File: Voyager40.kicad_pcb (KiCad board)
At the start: 2 copper layers, 244.5 x 76.2 mm, 192 parts, among them Q1 2N7002, SW1 5.2x5.2mm, U1 ATmega32U2-AU, U2 PRTR5V0U2X, Y1 16Mhz

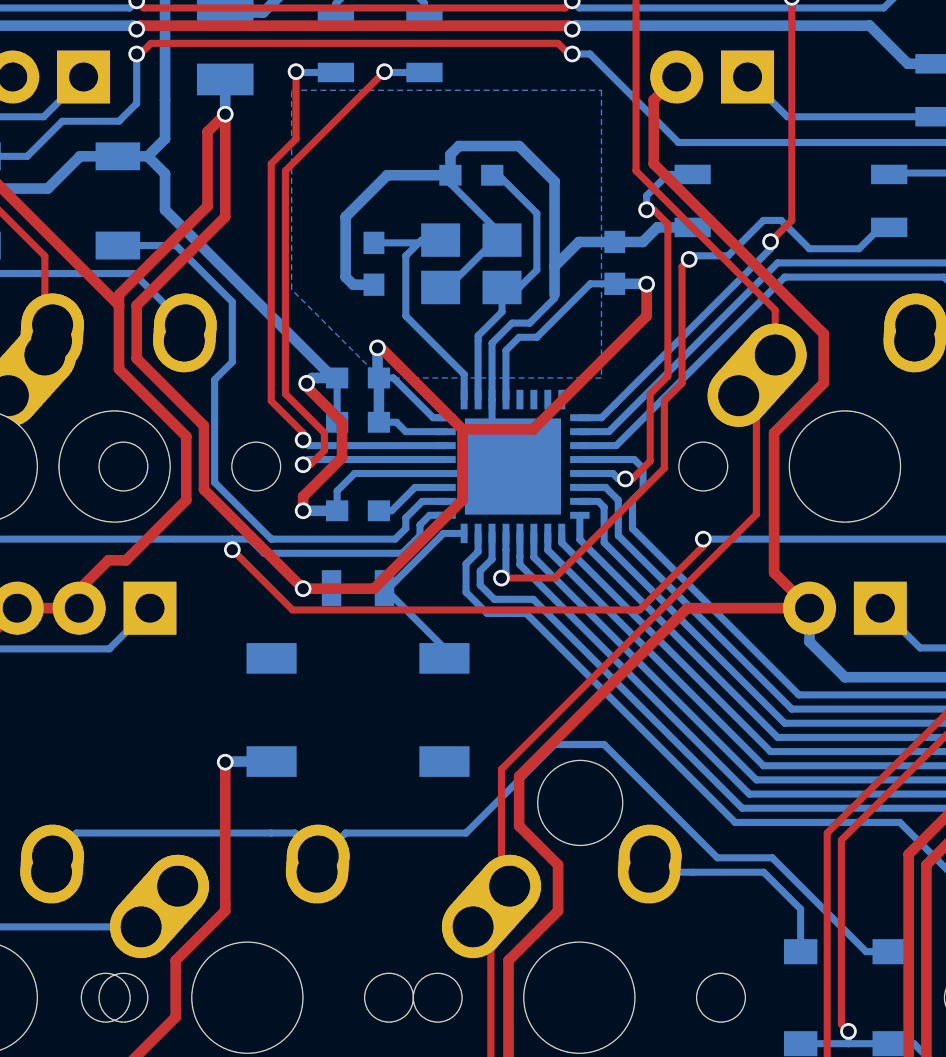
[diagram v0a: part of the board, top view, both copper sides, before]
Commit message: Repair the column traces
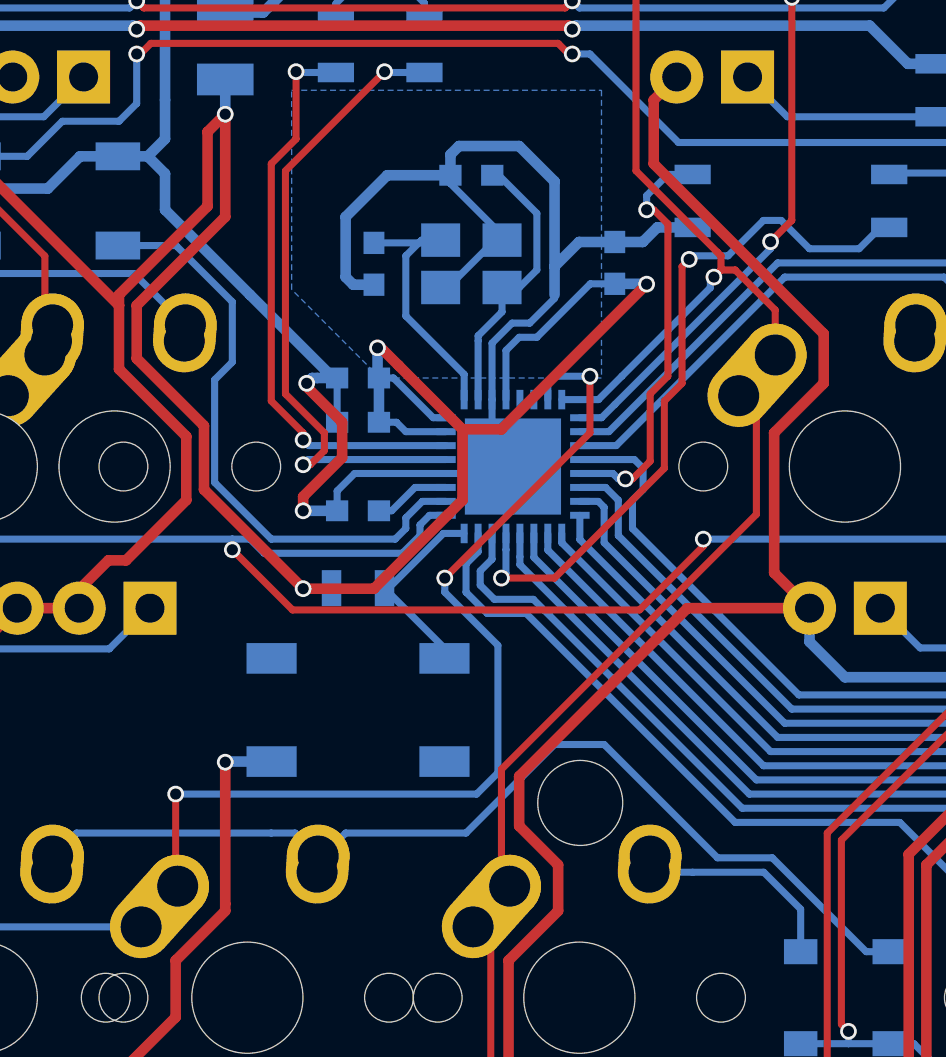
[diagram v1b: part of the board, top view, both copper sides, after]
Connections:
- U1 pad 7: Net-(U1-Pad7) -> COL0
- U1 pad 8: Net-(U1-Pad8) -> COL1
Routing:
- net COL0: track 75.0 -> 109.6 mm, vias 0 -> 3
- net COL1: track 61.8 -> 69.8 mm, vias 0 -> 1
- net +5V: track 1291.5 -> 1290.8 mm
